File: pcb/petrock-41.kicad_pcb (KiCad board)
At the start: 2 copper layers, 242.5 x 87.9 mm, 100 parts, among them J1 MJ-4PP-9, J2 OLED, J3 MJ-4PP-9, J4 OLED, SW1 SW_PUSH, SW10 SW_PUSH, SW11 SW_PUSH, SW12 SW_PUSH, SW13 SW_PUSH, SW14 SW_PUSH, SW15 SW_PUSH, SW16 SW_PUSH, SW17 SW_PUSH, SW18 SW_PUSH, SW19 SW_PUSH, SW2 SW_PUSH, SW20 SW_PUSH, SW21 SW_PUSH, SW22 SW_PUSH, SW23 SW_PUSH, SW24 SW_PUSH, SW25 SW_PUSH, SW26 SW_PUSH, SW27 SW_PUSH, SW29 SW_PUSH, SW3 SW_PUSH, SW30 SW_PUSH, SW31 SW_PUSH, SW32 SW_PUSH, SW33 SW_PUSH, SW34 SW_PUSH, SW35 SW_PUSH, SW36 SW_PUSH, SW37 SW_PUSH, SW38 SW_PUSH, SW39 SW_PUSH, SW4 SW_PUSH, SW41 SW_PUSH, SW42 SW_PUSH, SW43 SW_PUSH, SW44 SW_PUSH, SW5 SW_PUSH, SW6 SW_PUSH, SW8 SW_PUSH, SW9 SW_PUSH, U1 ProMicro, U2 ProMicro

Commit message: Wireless-ready pins, last-resort routing, fresh renders
The trackpoint moves to controller pins 1/2 (a nice!nano's high-frequency
D1/D0, as the ZMK PS/2 driver recommends) and each TRRS data line to pin
11 (tools/pins.py); wired QMK on an RP2040 handles both. A connection
boxed in by stock copper may now rip it up as a last resort, so both
boards route fully. README documents the wired and wireless pinouts.
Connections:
- U1 pad 11: unconnected-(U1-8/B4-Pad11) -> data
- U1 pad 2: data -> (no net)
- U2 pad 1: (no net) -> TP_CLK
- U2 pad 11: TP_DATA -> data_r
- U2 pad 12: TP_CLK -> unconnected-(U2-9/B5-Pad12)
- U2 pad 2: data_r -> TP_DATA
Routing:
- net VDD: track 79.0 -> 116.8 mm, vias 5 -> 10
- net reset_r: track 15.6 -> 42.5 mm, vias 1 -> 0
- net data_r: track 21.1 -> 46.7 mm, vias 1 -> 0
- net TP_CLK: track 42.5 -> 67.7 mm
- net TP_DATA: track 45.6 -> 68.5 mm
- net col1: track 153.2 -> 173.0 mm, vias 4 -> 5
- net data: track 9.25 -> 27.2 mm
- net GND: track 495.8 -> 479.5 mm, vias 11 -> 9
- net row0: track 139.2 -> 127.2 mm, vias 3 -> 0
- net col1_r: track 178.9 -> 170.5 mm, vias 5 -> 4
- net col0: track 162.8 -> 170.0 mm
- net row3: track 166.1 -> 161.4 mm
- net col4_r: track 132.0 -> 135.3 mm
- net col5_r: track 111.0 -> 107.8 mm
- net GNDA: track 449.6 -> 447.1 mm
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
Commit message: Hand-solder gaps of 0.9 mm, pinned tools, clean pours
Every hand-soldered pad now leaves at least 0.9 mm to the next (headers
stay at the standard 2.54 mm pitch): trackpoint sensor-link pads 1.6 mm
wide, driver host pads 0.9 mm, TRRS slot pads 2.1 mm long.

Pours drop floating islands. The last-resort routing pass repeats until
nothing is open. KiCad, Python and friends are pinned as GC roots in
.nix/ (bin/setup), so garbage collection can't break the build again.
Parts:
- moved RSW2 0.20 mm to (162.0, 80.4)
- moved RSW1 0.20 mm to (149.7, 80.4)
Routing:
- net row0: track 127.2 -> 131.3 mm
- net VDD: track 116.8 -> 119.3 mm
- net VCC: track 68.0 -> 66.3 mm, vias 4 -> 3

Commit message: Trackpoint driver host pads that fit both the drawing and the real board
The datasheet's 3.08 mm runs to pin 1's pad edge, not its centre, and its
1.80 mm pitch disagrees with holykeebs' photos of the Rev A board (1.72 mm,
scale-checked against the 2.5 mm link pads). Both agree on the row's middle,
so the host pads now sit at 1.758 mm pitch about it: every pin within 0.20 mm
of its pad's centre whichever is right. Pads 0.85 mm wide, gaps 0.9 mm.
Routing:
- net col0: track 170.0 -> 151.6 mm, vias 13 -> 6
- net GND: track 479.2 -> 489.2 mm, vias 9 -> 10
- net col4_r: track 135.3 -> 143.8 mm, vias 3 -> 5
- net row1: track 151.8 -> 157.8 mm, vias 10 -> 8
- net col1: track 173.0 -> 168.0 mm, vias 5 -> 9
- net row3: track 161.4 -> 166.1 mm
- net col1_r: track 170.6 -> 175.0 mm
- net col3_r: track 126.9 -> 130.3 mm, vias 5 -> 3
- net col0_r: track 128.5 -> 131.0 mm, vias 7 -> 6
- net VDD: track 119.3 -> 118.4 mm, vias 10 -> 9
- net TP_CLK: track 67.6 -> 67.1 mm
- net VCC: vias 3 -> 4

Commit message: Evenly spaced controller corner with exact nice!nano and jack sizes
Keycap, controller, jack and edge now sit 1.63 mm apart, and the
controller's and jack's square top corners are 1.15 mm inside the slope,
square to it, like the keycaps. Sizes come from 3D models: the nice!nano's
board is 17.78 x 33.0 mm with its USB end 3.79 mm past the first pin; the
PJ320A body is 6.0 mm. The render stand-in controller now has those sizes.
drop_dangling also catches lengths DRC prints in exponent form.
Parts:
- moved J2 1.36 mm to (132.0, 97.0)
- moved U1 1.36 mm to (135.8, 78.5)
- moved J4 1.36 mm to (172.2, 97.0)
- moved U2 1.36 mm to (175.9, 78.5)
- moved J3 0.61 mm to (162.4, 61.2)
- moved J1 0.61 mm to (149.3, 61.2)
- moved RSW1 0.46 mm to (149.3, 80.3)
- moved RSW2 0.45 mm to (162.4, 80.3)
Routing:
- net col0_r: track 131.0 -> 83.3 mm
- net GNDA: track 446.7 -> 487.1 mm, vias 4 -> 5
- net GND: track 489.2 -> 512.8 mm, vias 10 -> 13
- net col1_r: track 175.0 -> 195.2 mm, vias 4 -> 5
- net data: track 27.3 -> 40.9 mm, vias 0 -> 1
- net VDD: track 118.4 -> 131.0 mm, vias 9 -> 7
- net row3: track 166.1 -> 156.0 mm, vias 3 -> 2
- net row1: track 157.8 -> 150.6 mm, vias 8 -> 6
- net col0: track 151.6 -> 157.5 mm, vias 6 -> 7
- net col4_r: track 143.8 -> 138.8 mm, vias 5 -> 8
- net col2: track 141.3 -> 145.8 mm, vias 4 -> 7
- net row0: track 131.3 -> 135.6 mm
- net col1: track 168.0 -> 170.7 mm, vias 9 -> 10
- net VCC: track 66.3 -> 64.6 mm, vias 4 -> 2
- net row1_r: track 85.7 -> 84.1 mm
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
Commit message: Five standoffs per half, logo on the board, plain controller corner
The standoff the outer pinky column lost moves to where the pinky and ring
columns meet, so the outer top corner is supported again (10 in all). The
logo is back on the board's silkscreen. The jack, reset button and OLED
header lose their printed outlines. The plate's opening by the controller
now starts at the inner index keycap line instead of the stock plate's
fixed edge, clearing the moved controller's sockets by 1.66 mm. The board
records its ENIG finish; renders can hide the jack and reset ("wireless").
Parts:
- added h2: h2, holykeebs:M2_SPACER, F.Cu at (53.8, 73.0)
- added h2: h2, holykeebs:M2_SPACER, B.Cu at (258.0, 73.0)
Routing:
- net col0: track 157.5 -> 201.5 mm, vias 7 -> 15
- net col0_r: track 83.3 -> 40.1 mm, vias 6 -> 3
- net VDD: track 131.0 -> 107.2 mm, vias 7 -> 10
- net GNDA: track 487.1 -> 465.0 mm
- net GND: track 512.8 -> 491.5 mm, vias 13 -> 10
- net col1_r: track 195.2 -> 186.0 mm, vias 5 -> 3
- net col3_r: track 130.0 -> 126.0 mm, vias 3 -> 5
- net col2: track 145.8 -> 143.2 mm, vias 7 -> 5
- net row3: track 156.0 -> 157.2 mm
- net col4_r: track 138.8 -> 137.8 mm, vias 8 -> 6
- net col1: track 170.7 -> 169.7 mm, vias 10 -> 6
- net row3_r: track 157.2 -> 158.1 mm

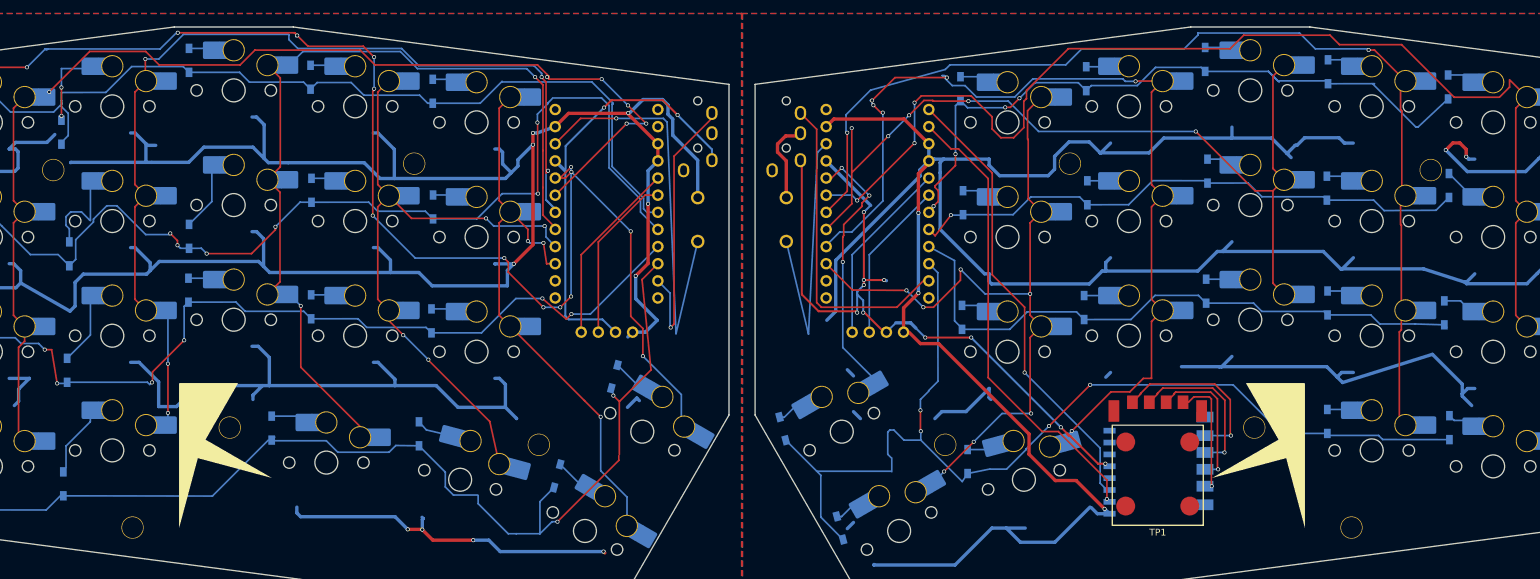
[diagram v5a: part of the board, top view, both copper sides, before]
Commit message: Standoffs placed by geometry
Each standoff between four keys sits at the four keys' centre (midway
between the columns and between their staggered row gaps): pinky and
ring top and bottom, index and inner index at the top. The thumb one
is equally far from its three keycap corners, and the one by the
trackpoint sits at the centre of the key cell the logo's notch outlines.
D29 moves 0.3 mm to make room and stays clear. Standoffs keep 1.5 mm
from the logo.
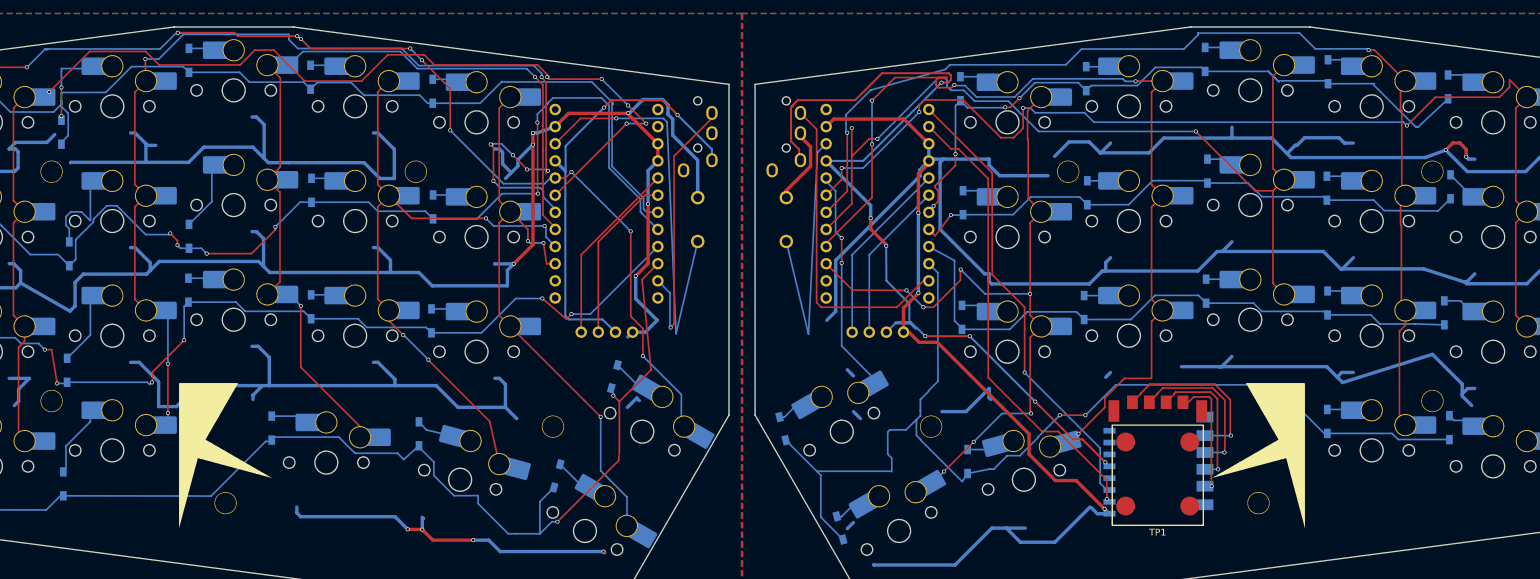
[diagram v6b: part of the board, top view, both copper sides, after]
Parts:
- moved h2 22.3 mm to (53.5, 107.2)
- moved h2 22.3 mm to (258.2, 107.2)
- moved h2 11.2 mm to (79.3, 122.4)
- moved h2 11.2 mm to (232.4, 122.4)
- moved h2 3.41 mm to (183.9, 111.0)
- moved h2 3.41 mm to (127.8, 111.0)
- moved ? 1.22 mm to (204.2, 73.2)
- moved ? 1.22 mm to (107.5, 73.2)
- moved h2 0.35 mm to (53.5, 73.2)
- moved h2 0.35 mm to (258.2, 73.2)
- moved D29 0.30 mm to (260.9, 75.5)
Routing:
- net col0: track 201.5 -> 165.1 mm, vias 15 -> 11
- net VDD: track 107.2 -> 128.3 mm, vias 10 -> 7
- net col2: track 143.2 -> 162.0 mm, vias 5 -> 9
- net GNDA: track 465.0 -> 482.4 mm
- net GND: track 491.5 -> 475.0 mm
- net col1_r: track 186.0 -> 175.1 mm, vias 3 -> 4
- net col0_r: track 40.1 -> 32.6 mm, vias 3 -> 2
- net col1: track 169.7 -> 172.9 mm
- net col3_r: track 126.0 -> 128.4 mm, vias 5 -> 3
- net col4_r: track 137.8 -> 139.0 mm, vias 6 -> 5
- net row3_r: track 158.1 -> 157.7 mm, vias 4 -> 2
